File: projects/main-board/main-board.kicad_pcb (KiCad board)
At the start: 6 copper layers, 174 x 75.9 mm, 221 parts, among them J1 TC2030, J2 TC2030, J3 S3B-PH-SM4-TB, J4 USB4105-GF-A, J5 TC2030, J6 NHD-4.3-480272EF-ASXP (Molex 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, J7 USB4105-GF-A, Q1 ZXTN4240F-7, Q2 ZXTN4240F-7, SW1 450404015514, SW10 TS06-667-25-BK-160-G-SMT-TR, SW11 TS06-667-25-BK-160-G-SMT-TR, SW12 TS06-667-25-BK-160-G-SMT-TR, SW18 TS06-667-25-BK-160-G-SMT-TR, SW2 TS06-667-25-BK-160-G-SMT-TR, SW3 TS06-667-25-BK-160-G-SMT-TR, SW4 TS06-667-25-BK-160-G-SMT-TR, SW5 TS06-667-25-BK-160-G-SMT-TR, SW6 TS06-667-25-BK-160-G-SMT-TR, SW9 TS06-667-25-BK-160-G-SMT-TR, U1 STM32N657X0HxQ, U10 AP5725WG-7, U11 NAU8325YG, U12 TLV74330PDBVR, U13 DM3AT-SF-PEJM5, U14 LSM6DSO32TR, U2 APS256XXN-OBR-BG, U3 MX25UM25645GXDI00, U4 TPS22992RXPR, U5 MPM3805GQB-18-Z, U6 TPSM863253RDXR, U7 MAX77972EWX+T, U8 TS3USB221ARSER, U9 ESP32-C6FH4, Y1 ABM10W-40.0000MHZ-8-B1U-T3, Y2 ABM11W-48.0000MHZ-8-K1Z-T3, Y3 ABS06-32.768KHZ-9-1-T

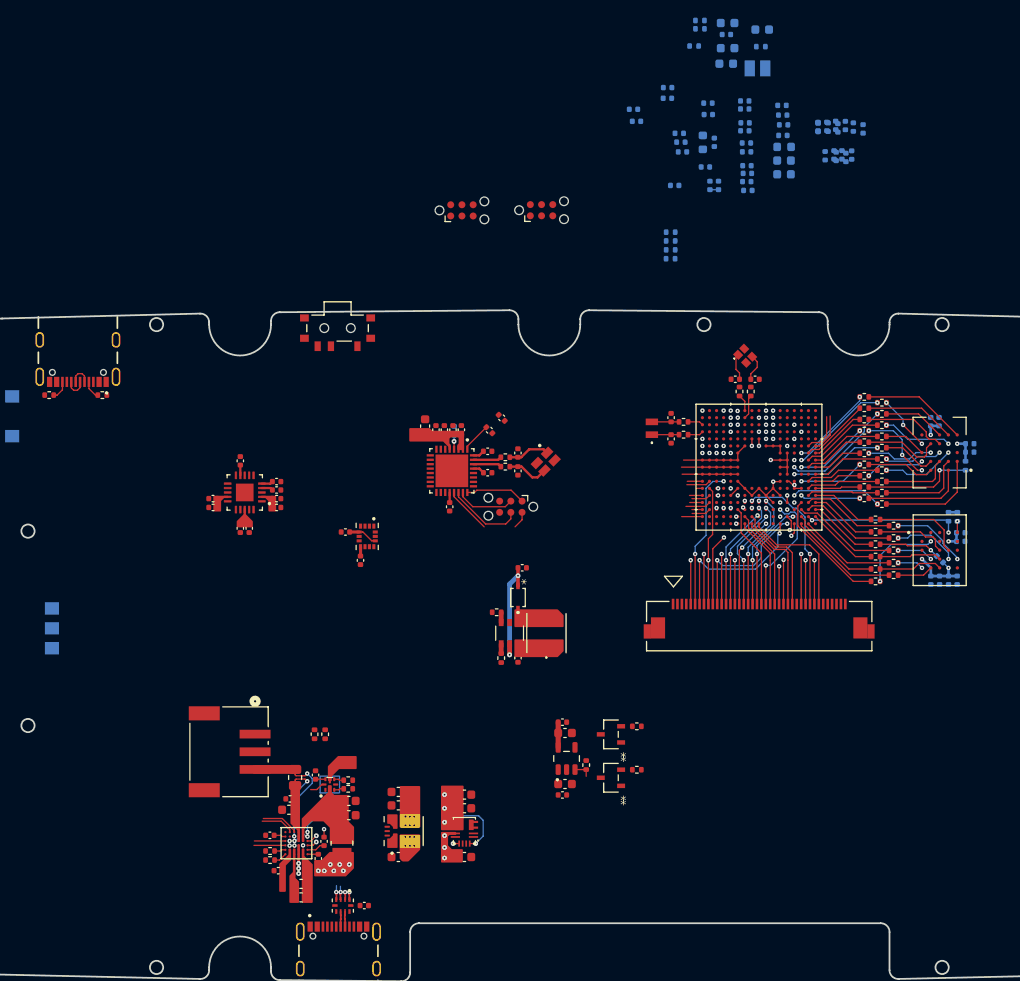
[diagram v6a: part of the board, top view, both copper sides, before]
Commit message: More routing of main board
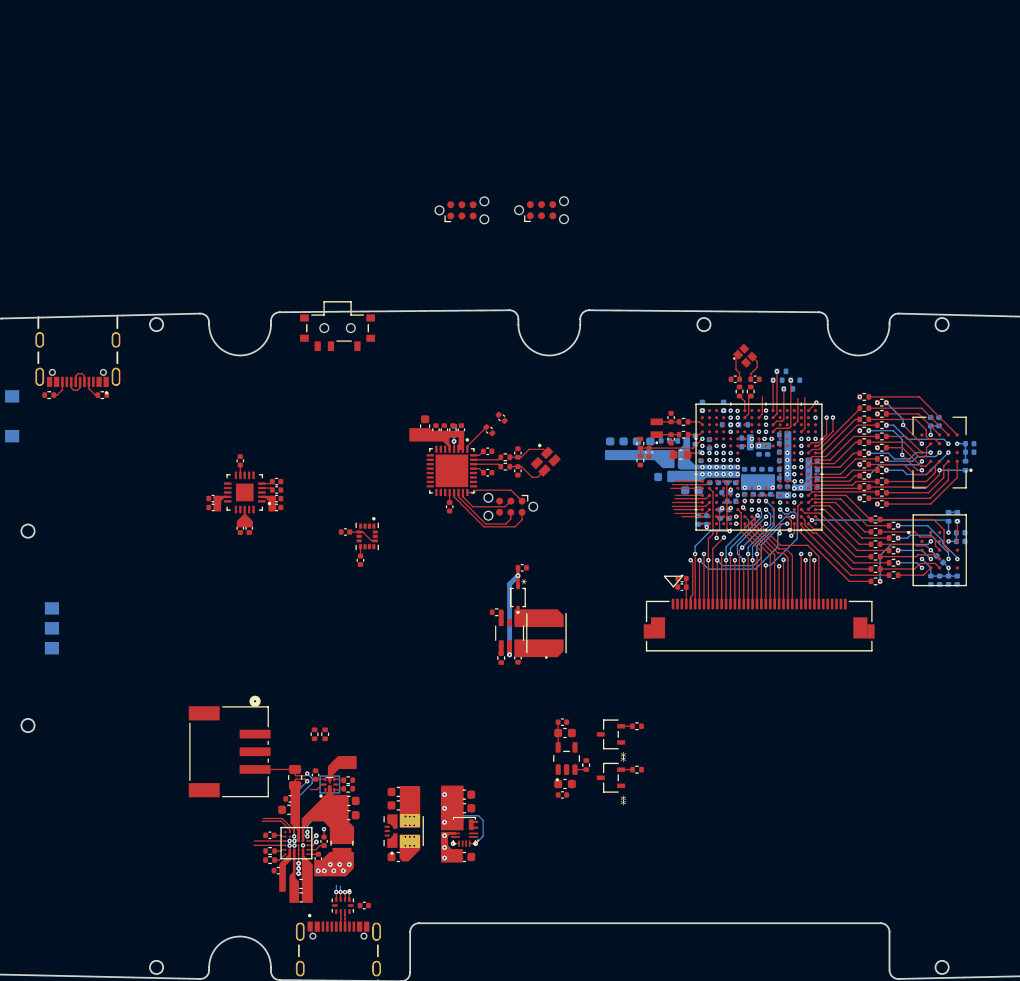
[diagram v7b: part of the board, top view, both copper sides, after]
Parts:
- C12, C89, C90, L2, R3, R4: moved to F.Cu
- moved C90 56.6 mm to (166.8, 94.2)
- moved C89 54.4 mm to (166.8, 93.2)
- moved R4 50.3 mm to (162.0, 79.9), turned to -90 degrees
- moved C11 49.2 mm to (161.7, 78.5), turned to 90 degrees
- moved C35 49.0 mm to (163.2, 78.5), turned to 90 degrees
- moved R3 47.4 mm to (162.0, 77.9), turned to -90 degrees
- moved C19 46.8 mm to (160.1, 78.5), turned to 90 degrees
- moved C20 46.5 mm to (171.1, 85.9), turned to -90 degrees
- moved C3 46.5 mm to (164.9, 77.6)
- moved R1 45.5 mm to (166.8, 77.6)
- moved C27 45.5 mm to (158.6, 78.5), turned to 90 degrees
- moved C6 45.3 mm to (172.1, 85.9), turned to -90 degrees
- moved L1 45.2 mm to (166.1, 79.7)
- moved C41 44.3 mm to (177.8, 83.3), turned to 90 degrees
- moved C45 43.5 mm to (178.7, 83.3), turned to 90 degrees
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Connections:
- C13 pad 1: Net-(C13-Pad1) -> VDDA18PMU
- C16 pad 1: Net-(C16-Pad1) -> VDDSMPS
- C24 pad 1: Net-(C16-Pad1) -> VDDSMPS
- C32 pad 1: Net-(C16-Pad1) -> VDDSMPS
- C39 pad 1: Net-(C16-Pad1) -> VDDSMPS
- C44 pad 1: Net-(C16-Pad1) -> VDDSMPS
- C47 pad 1: Net-(C16-Pad1) -> VDDSMPS
- L2 pad 1: VDDA18PMU -> 1V8
- L2 pad 2: Net-(C13-Pad1) -> VDDA18PMU
- L3 pad 1: VDDSMPS -> 1V8
- L3 pad 2: Net-(C16-Pad1) -> VDDSMPS
- U1 pad A16: unconnected-(U1E-PE9-PadA16) -> /MCU/MOTOR_PWR_EN
- U1 pad B1: unconnected-(U1H-PH3-PadB1) -> /Buttons/BUTTONS.B5
- U1 pad B17: unconnected-(U1B-PB14-PadB17) -> /MCU/ESP32_EN
- U1 pad B2: unconnected-(U1H-PH6-PadB2) -> /Buttons/BUTTONS.B8
- U1 pad F13: /MCU/ESP32_EN -> unconnected-(U1B-PB3-PadF13)
- U1 pad M3: /Buttons/BUTTONS.B5 -> unconnected-(U1F-PF5-PadM3)
- U1 pad N3: /Buttons/BUTTONS.B8 -> unconnected-(U1F-PF8-PadN3)
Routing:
- net GND: track 12.5 -> 0.92 mm, vias 1 -> 6
- net VDDCORE: track 9.49 -> 0.10 mm, vias 2 -> 4
- net Net-(U1K-VBAT): track 0.00 -> 8.44 mm
- net /Audio/I2C.SDA: track 0.00 -> 7.50 mm
- net Net-(L1-Pad1): track 6.38 -> 0.00 mm, vias 0 -> 6
- net VDDSMPS: track 6.30 -> 0.00 mm, vias 0 -> 6
- net /MCU/I2C4.SDA: track 4.25 -> 9.67 mm
- net 1V8: track 29.6 -> 24.5 mm, vias 10 -> 13
- net /Audio/I2C.SCL: track 0.00 -> 4.93 mm
- net /LCD/LCD.VSYNC: track 23.0 -> 18.8 mm
- net /MCU/DEBUG_UART.TX: track 0.00 -> 4.08 mm, vias 1 -> 0
- net /Buttons/BUTTONS.B0: track 0.00 -> 3.50 mm
- net /MCU/I2C4.SCL: track 3.79 -> 7.24 mm
- net /ESP32/ESP32_UART.TX: track 12.0 -> 15.3 mm, vias 0 -> 1
- net /MCU/DEBUG_UART.RX: track 0.00 -> 3.15 mm, vias 1 -> 0
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
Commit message: WIP splitting main board into 3
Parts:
- removed SW10, SW11, SW12, SW18, SW2, SW3, SW4, SW5, SW6, SW9: TS06-667-25-BK-160-G-SMT-TR, footprint-library:TS06-667-25-BK-160-G-SMT-TR
- added J8: 5051101292, footprint-library:5051101292, F.Cu at (196.4, 102.3)
- added J9: 5051101292, footprint-library:5051101292, F.Cu at (107.1, 102.3)
- moved U13 85.2 mm to (151.6, 68.7), turned to 180 degrees
- moved C105 72.6 mm to (151.1, 78.7), turned to -90 degrees
- moved C104 72.0 mm to (152.1, 78.7), turned to -90 degrees
- moved J4 70.7 mm to (113.1, 135.4), turned to 0 degrees
- moved R60 69.0 mm to (157.5, 78.7), turned to 90 degrees
- moved R53 60.5 mm to (116.4, 129.1), turned to 0 degrees
- moved R51 57.4 mm to (110.3, 129.1), turned to 180 degrees
- moved J2 47.6 mm to (186.1, 69.1)
- moved C87 41.9 mm to (183.6, 124.7)
- moved L6 41.9 mm to (186.8, 121.9)
- moved R55 41.9 mm to (181.7, 124.7)
- moved C88 41.9 mm to (184.0, 114.5)
- moved D1 41.9 mm to (183.6, 117.8)
- moved R56 41.9 mm to (181.1, 119.5)
- moved U10 41.9 mm to (182.6, 121.9)
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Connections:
- net /Haptics/LEFT_MOTOR_N renamed /Controllers/LEFT_MOTOR.N
- net /Haptics/MOTOR_P renamed /Controllers/LEFT_MOTOR.P
- net /MCU/BACKLIGHT_PWM renamed /LCD/BACKLIGHT_PWM
- net /MCU/LEFT_MOTOR_PWM renamed /Haptics/LEFT_MOTOR_EN
- net /MCU/MOTOR_PWR_EN renamed /Haptics/MOTOR_PWR_EN
- net /MCU/RIGHT_MOTOR_PWM renamed /Haptics/RIGHT_MOTOR_EN
- net /Power/CC1 renamed /USB/USB_CC1
- net /Power/CC2 renamed /USB/USB_CC2
- Q2 pad 1: /Haptics/RIGHT_MOTOR_N -> /Controllers/RIGHT_MOTOR.N
- U1 pad B1: /Buttons/BUTTONS.B5 -> /Controllers/BUTTONS.B5
- U1 pad B2: /Buttons/BUTTONS.B8 -> /Controllers/BUTTONS.B8
- U1 pad F4: /Buttons/BUTTONS.B3 -> /Controllers/BUTTONS.B3
- U1 pad L1: /Buttons/BUTTONS.B6 -> /Controllers/BUTTONS.B6
- U1 pad L2: /Buttons/BUTTONS.B4 -> /Controllers/BUTTONS.B4
- U1 pad M1: /Buttons/BUTTONS.B7 -> /Controllers/BUTTONS.B7
- U1 pad P1: /Buttons/BUTTONS.B9 -> /Controllers/BUTTONS.B9
- U1 pad P2: /Buttons/BUTTONS.B2 -> /Controllers/BUTTONS.B2
- U1 pad R3: /Buttons/BUTTONS.B0 -> /Controllers/BUTTONS.B0
- U1 pad T1: /Buttons/BUTTONS.B1 -> /Controllers/BUTTONS.B1
- U11 pad 1: /Audio/RIGHT_SPEAKER_N -> /Audio/RIGHT_SPEAKER.N
- U11 pad 15: /Audio/LEFT_SPEAKER_P -> /Audio/LEFT_SPEAKER.P
- U11 pad 17: /Audio/LEFT_SPEAKER_N -> /Audio/LEFT_SPEAKER.N
- U11 pad 19: /Audio/RIGHT_SPEAKER_P -> /Audio/RIGHT_SPEAKER.P
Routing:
- net VBAT: track 15.4 -> 10.9 mm
- net /Controllers/BUTTONS.B2: track 0.00 -> 4.42 mm
- net /Buttons/BUTTONS.B2: track 4.42 -> 0.00 mm
- net /Controllers/BUTTONS.B4: track 0.00 -> 4.40 mm
- net /Buttons/BUTTONS.B4: track 4.40 -> 0.00 mm
- net /Controllers/BUTTONS.B7: track 0.00 -> 3.58 mm
- net /Buttons/BUTTONS.B7: track 3.58 -> 0.00 mm
- net /Controllers/BUTTONS.B0: track 0.00 -> 3.50 mm, vias 0 -> 1
- net /Buttons/BUTTONS.B0: track 3.50 -> 0.00 mm, vias 1 -> 0
- net /Controllers/BUTTONS.B9: track 0.00 -> 3.43 mm
- net /Buttons/BUTTONS.B9: track 3.43 -> 0.00 mm
- net /Controllers/BUTTONS.B6: track 0.00 -> 3.24 mm
- net /Buttons/BUTTONS.B6: track 3.24 -> 0.00 mm
- net /Controllers/BUTTONS.B1: track 0.00 -> 2.35 mm
- net /Buttons/BUTTONS.B1: track 2.35 -> 0.00 mm
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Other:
- board size 174 x 75.9 mm -> 104.8 x 77 mm
